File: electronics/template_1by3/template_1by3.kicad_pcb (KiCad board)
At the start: 2 copper layers, 19 x 49 mm, 10 parts, among them J1 1, J2 2, J3 3, J4 4, J5 5, J6 6, J7 7, J8 8

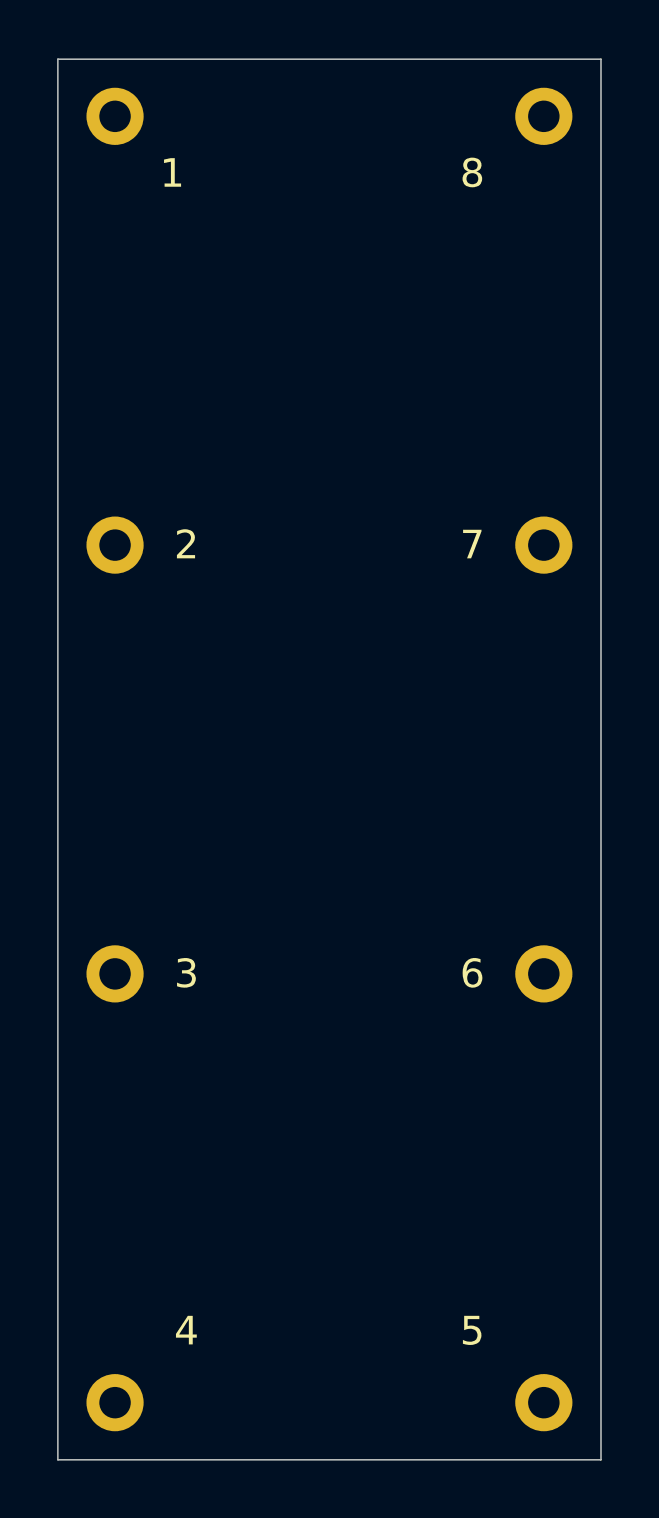
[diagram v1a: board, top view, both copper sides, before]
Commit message: changed font size on the templates
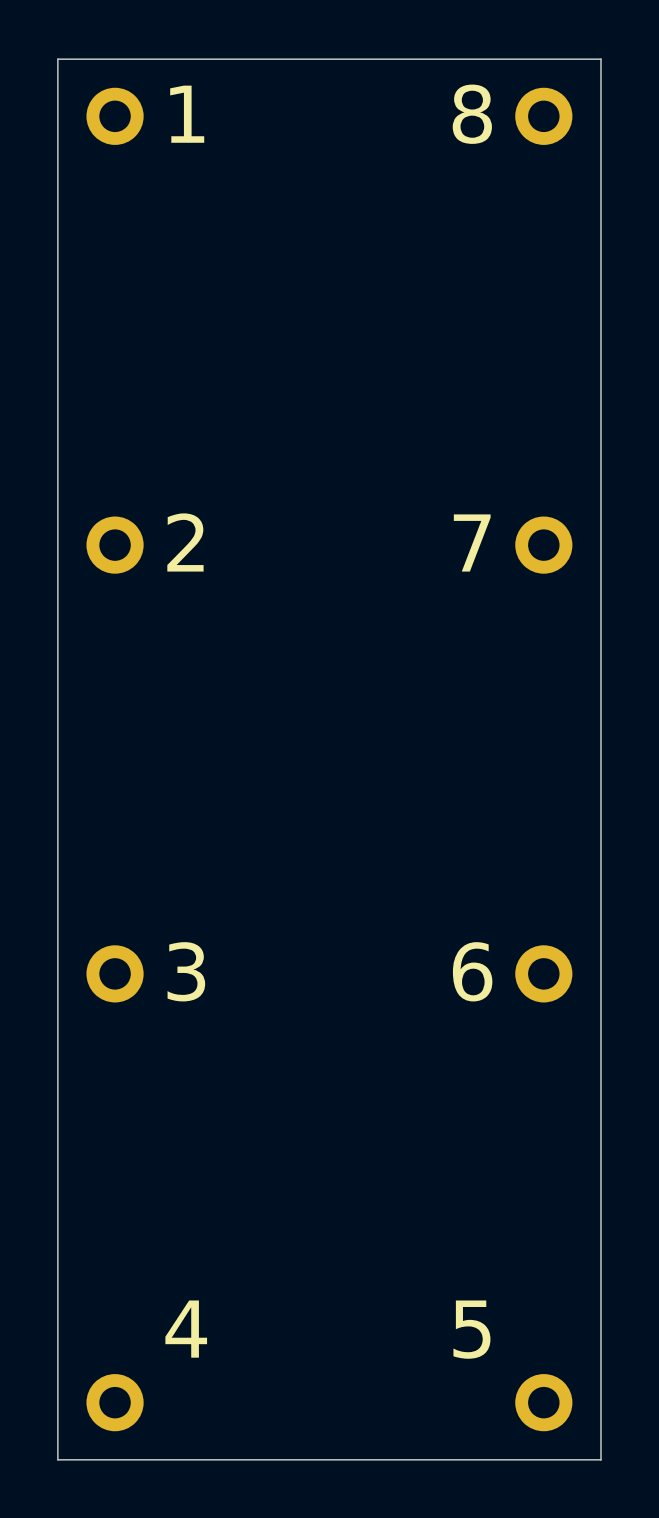
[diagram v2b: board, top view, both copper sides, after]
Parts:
- N1: value 20201119 -> V20220113
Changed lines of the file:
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@@
-(kicad_pcb (version 20171130) (host pcbnew 5.1.8-db9833491~87~ubuntu20.04.1)
+(kicad_pcb (version 20171130) (host pcbnew 5.99.0+really5.1.10+dfsg1-1)
   (general
     (thickness 1.6)
@@
       (effects (font (size 1 1) (thickness 0.15)))
     )
-    (fp_text value 8 (at -2.5 2) (layer F.SilkS)
-      (effects (font (size 1 1) (thickness 0.15)))
+    (fp_text value 8 (at -2.5 0) (layer F.SilkS)
+      (effects (font (size 2 2) (thickness 0.3)))
     )
     (fp_circle (center 0 0) (end 1.3 0) (layer B.CrtYd) (width 0.025))
@@
     )
     (fp_text value 7 (at -2.5 0) (layer F.SilkS)
-      (effects (font (size 1 1) (thickness 0.15)))
+      (effects (font (size 2 2) (thickness 0.3)))
     )
     (fp_circle (center 0 0) (end 1.3 0) (layer B.CrtYd) (width 0.025))
@@
     )
     (fp_text value 6 (at -2.5 0) (layer F.SilkS)
-      (effects (font (size 1 1) (thickness 0.15)))
+      (effects (font (size 2 2) (thickness 0.3)))
     )
     (fp_circle (center 0 0) (end 1.3 0) (layer F.CrtYd) (width 0.025))
@@
     )
     (fp_text value 5 (at -2.5 -2.5) (layer F.SilkS)
-      (effects (font (size 1 1) (thickness 0.15)))
+      (effects (font (size 2 2) (thickness 0.3)))
     )
     (fp_circle (center 0 0) (end 1.3 0) (layer F.CrtYd) (width 0.025))
@@
     )
     (fp_text value 4 (at 2.5 -2.5) (layer F.SilkS)
-      (effects (font (size 1 1) (thickness 0.15)))
+      (effects (font (size 2 2) (thickness 0.3)))
     )
     (fp_circle (center 0 0) (end 1.3 0) (layer B.CrtYd) (width 0.025))
@@
     )
     (fp_text value 3 (at 2.5 0) (layer F.SilkS)
-      (effects (font (size 1 1) (thickness 0.15)))
+      (effects (font (size 2 2) (thickness 0.3)))
     )
     (fp_circle (center 0 0) (end 1.3 0) (layer B.CrtYd) (width 0.025))
@@
     )
     (fp_text value 2 (at 2.5 0) (layer F.SilkS)
-      (effects (font (size 1 1) (thickness 0.15)))
+      (effects (font (size 2 2) (thickness 0.3)))
     )
     (fp_circle (center 0 0) (end 1.3 0) (layer B.CrtYd) (width 0.025))
@@
       (effects (font (size 1 1) (thickness 0.15)))
     )
-    (fp_text value 1 (at 2 2) (layer F.SilkS)
-      (effects (font (size 1 1) (thickness 0.15)))
+    (fp_text value 1 (at 2.5 0) (layer F.SilkS)
+      (effects (font (size 2 2) (thickness 0.3)))
     )
     (fp_circle (center 0 0) (end 1.3 0) (layer B.CrtYd) (width 0.025))
@@
       (effects (font (size 1 1) (thickness 0.15)) (justify mirror))
     )
-    (fp_text value 20201119 (at 0.8 0.1) (layer B.SilkS)
+    (fp_text value V20220113 (at 0.8 0.1) (layer B.SilkS)
       (effects (font (size 0.8 0.8) (thickness 0.15)) (justify mirror))
     )

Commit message: converted template 1by3 to kicad 7
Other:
- net class Default removed
- rule pad_to_mask_clearance: 0.0762 -> 0
